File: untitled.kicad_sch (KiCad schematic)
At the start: 2 parts, among them U5 MS5611-01BA

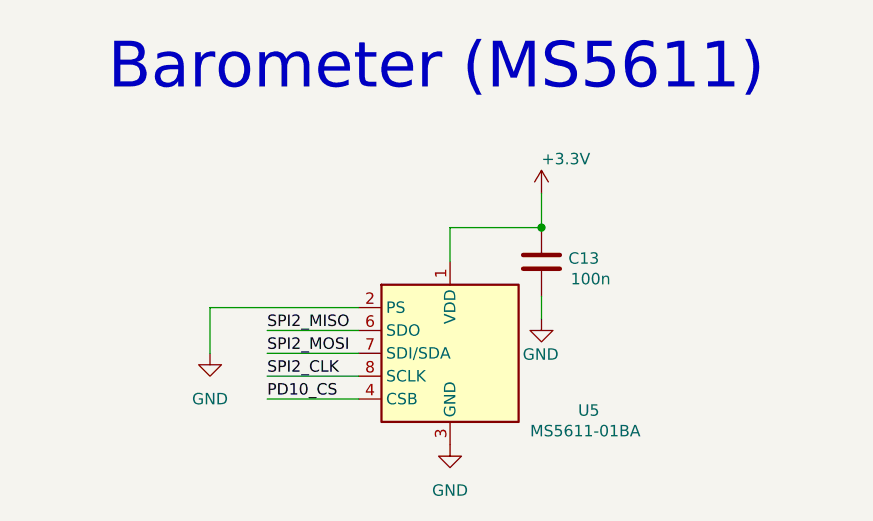
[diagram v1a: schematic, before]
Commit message: Feat: added Canbus
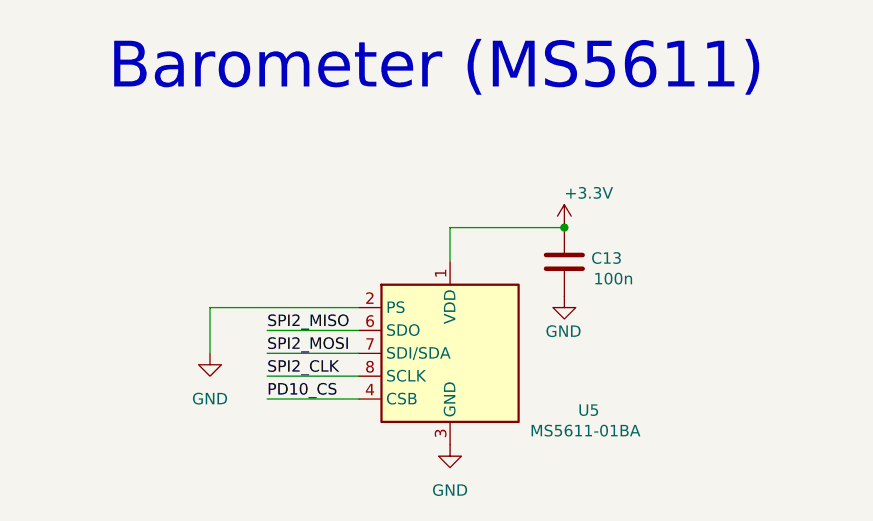
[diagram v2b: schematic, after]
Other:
- moved on the sheet: C13
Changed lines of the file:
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@@
 	)
 	(junction
-		(at 144.78 87.63)
+		(at 147.32 87.63)
 		(diameter 0)
 		(color 0 0 0 0)
@@
 	(wire
 		(pts
-			(xy 144.78 95.25) (xy 144.78 97.79)
-		)
-		(stroke
-			(width 0)
-			(type default)
-		)
-	)
-	(wire
-		(pts
 			(xy 114.3 106.68) (xy 124.46 106.68)
 		)
@@
 	(wire
 		(pts
-			(xy 134.62 87.63) (xy 144.78 87.63)
-		)
-		(stroke
-			(width 0)
-			(type default)
-		)
-	)
-	(wire
-		(pts
-			(xy 144.78 83.82) (xy 144.78 87.63)
+			(xy 134.62 87.63) (xy 147.32 87.63)
 		)
 		(stroke
@@
 	(symbol
 		(lib_id "power:+3.3V")
-		(at 144.78 83.82 0)
+		(at 147.32 87.63 0)
 		(unit 1)
 		(body_style 1)
@@
 		(dnp no)
 		(property "Reference" "#PWR024"
-			(at 144.78 87.63 0)
+			(at 147.32 91.44 0)
 			(hide yes)
 			(show_name no)
@@
 		)
 		(property "Value" "+3.3V"
-			(at 144.7801 80.01 0)
+			(at 147.3201 83.82 0)
 			(show_name no)
 			(do_not_autoplace no)
@@
 		)
 		(property "Footprint" ""
-			(at 144.78 83.82 0)
+			(at 147.32 87.63 0)
 			(hide yes)
 			(show_name no)
@@
 		)
 		(property "Datasheet" ""
-			(at 144.78 83.82 0)
+			(at 147.32 87.63 0)
 			(hide yes)
 			(show_name no)
@@
 		)
 		(property "Description" "Power symbol creates a global label with name \"+3.3V\""
-			(at 144.78 83.82 0)
+			(at 147.32 87.63 0)
 			(hide yes)
 			(show_name no)
@@
 	(symbol
 		(lib_id "Device:C")
-		(at 144.78 91.44 0)
+		(at 147.32 91.44 0)
 		(unit 1)
 		(body_style 1)
@@
 		(dnp no)
 		(property "Reference" "C13"
-			(at 149.479 91.059 0)
+			(at 152.019 91.059 0)
 			(show_name no)
 			(do_not_autoplace no)
@@
 		)
 		(property "Value" "100n"
-			(at 150.241 93.345 0)
+			(at 152.781 93.345 0)
 			(show_name no)
 			(do_not_autoplace no)
@@
 		)
 		(property "Footprint" ""
-			(at 145.7452 95.25 0)
+			(at 148.2852 95.25 0)
 			(hide yes)
 			(show_name no)
@@
 		)
 		(property "Datasheet" ""
-			(at 144.78 91.44 0)
+			(at 147.32 91.44 0)
 			(hide yes)
 			(show_name no)
@@
 		)
 		(property "Description" "Unpolarized capacitor"
-			(at 144.78 91.44 0)
+			(at 147.32 91.44 0)
 			(hide yes)
 			(show_name no)
@@
 	(symbol
 		(lib_id "power:GND")
-		(at 144.78 97.79 0)
+		(at 147.32 95.25 0)
 		(unit 1)
 		(body_style 1)
@@
 		(dnp no)
 		(property "Reference" "#PWR025"
-			(at 144.78 104.14 0)
+			(at 147.32 101.6 0)
 			(hide yes)
 			(show_name no)
@@
 		)
 		(property "Value" "GND"
-			(at 146.685 101.727 0)
+			(at 149.225 99.187 0)
 			(show_name no)
 			(do_not_autoplace no)
@@
 		)
 		(property "Footprint" ""
-			(at 144.78 97.79 0)
+			(at 147.32 95.25 0)
 			(hide yes)
 			(show_name no)
@@
 		)
 		(property "Datasheet" ""
-			(at 144.78 97.79 0)
+			(at 147.32 95.25 0)
 			(hide yes)
 			(show_name no)
@@
 		)
 		(property "Description" "Power symbol creates a global label with name \"GND\" , ground"
-			(at 144.78 97.79 0)
-			(hide yes)
-			(show_name no)
+			(at 147.32 95.25 0)
+			(hide yes)
+			(show_name no)
